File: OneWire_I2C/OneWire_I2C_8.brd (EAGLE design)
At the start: 25.4 x 35.6 mm, 25 parts, among them U1 P82B715D

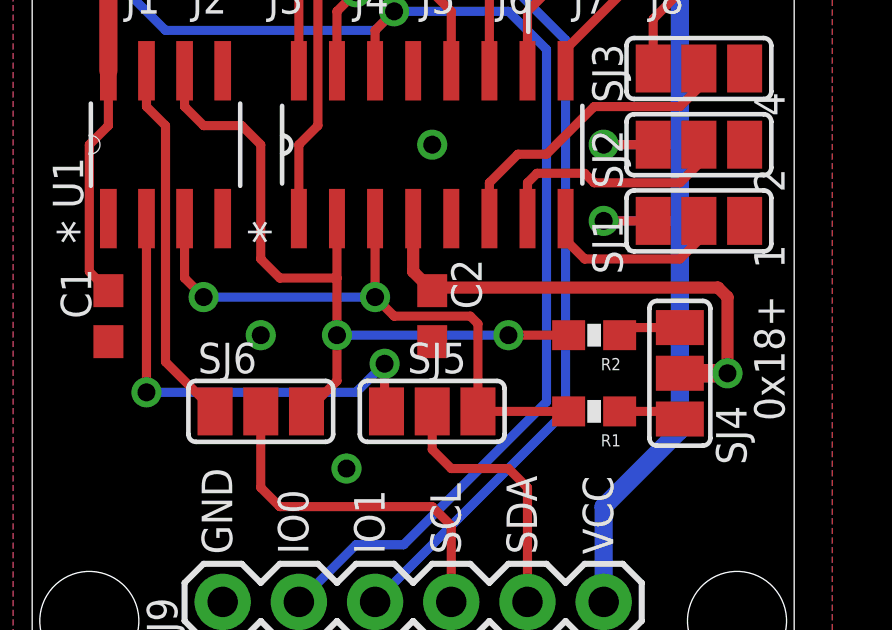
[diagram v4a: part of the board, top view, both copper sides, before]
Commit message: Added Raspberry pi board, updated I2C extender pullup resistors to other boards
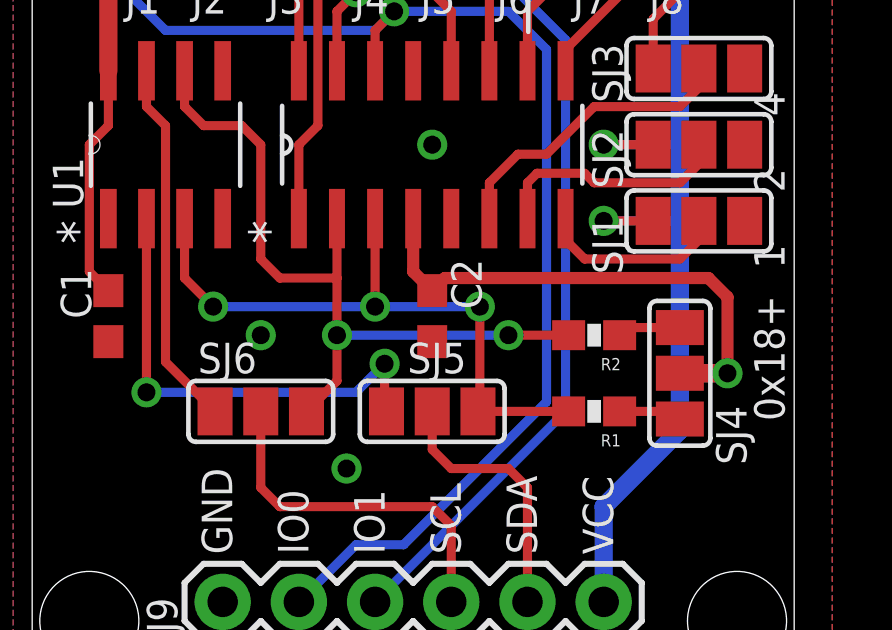
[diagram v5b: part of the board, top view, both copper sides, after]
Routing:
- net SDA: track 21.0 -> 21.7 mm, vias 2 -> 3
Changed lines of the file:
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@@
 <grid distance="0.025" unitdist="inch" unit="inch" style="dots" multiple="1" display="yes" altdistance="0.0125" altunitdist="inch" altunit="inch"/>
 <layers>
-<layer number="1" name="Top" color="4" fill="1" visible="no" active="yes"/>
+<layer number="1" name="Top" color="4" fill="1" visible="yes" active="yes"/>
 <layer number="2" name="Route2" color="1" fill="3" visible="no" active="no"/>
 <layer number="3" name="Route3" color="4" fill="3" visible="no" active="no"/>
@@
 <layer number="19" name="Unrouted" color="6" fill="1" visible="yes" active="yes"/>
 <layer number="20" name="Dimension" color="15" fill="1" visible="yes" active="yes"/>
-<layer number="21" name="tPlace" color="7" fill="1" visible="no" active="yes"/>
+<layer number="21" name="tPlace" color="7" fill="1" visible="yes" active="yes"/>
 <layer number="22" name="bPlace" color="7" fill="1" visible="yes" active="yes"/>
 <layer number="23" name="tOrigins" color="15" fill="1" visible="yes" active="yes"/>
@@
 <layer number="49" name="Reference" color="7" fill="1" visible="no" active="yes"/>
 <layer number="50" name="dxf" color="7" fill="1" visible="no" active="no"/>
-<layer number="51" name="tDocu" color="14" fill="1" visible="yes" active="yes"/>
+<layer number="51" name="tDocu" color="14" fill="1" visible="no" active="yes"/>
 <layer number="52" name="bDocu" color="7" fill="1" visible="yes" active="yes"/>
 <layer number="53" name="tGND_GNDA" color="7" fill="9" visible="no" active="no"/>
@@
 <via x="19.05" y="15.24" extent="1-16" drill="0.6"/>
 <wire x1="19.05" y1="15.24" x2="21.59" y2="15.24" width="0.3048" layer="16"/>
-<wire x1="22.86" y1="13.0175" x2="23.1775" y2="12.7" width="0.4064" layer="1"/>
+<wire x1="22.5425" y1="13.335" x2="23.1775" y2="12.7" width="0.4064" layer="1"/>
 <wire x1="23.1775" y1="12.7" x2="23.1775" y2="10.16" width="0.4064" layer="1"/>
 <wire x1="1.905" y1="17.78" x2="2.54" y2="18.415" width="0.3048" layer="1"/>
@@
 <wire x1="20.701" y1="21.971" x2="20.701" y2="20.32" width="0.3048" layer="1"/>
 <contactref element="C2" pad="1"/>
-<wire x1="22.86" y1="13.0175" x2="13.4375" y2="13.0175" width="0.4064" layer="1"/>
-<wire x1="13.4375" y1="13.0175" x2="13.335" y2="12.915" width="0.4064" layer="1"/>
+<wire x1="22.5425" y1="13.335" x2="13.755" y2="13.335" width="0.4064" layer="1"/>
+<wire x1="13.755" y1="13.335" x2="13.335" y2="12.915" width="0.4064" layer="1"/>
 <wire x1="12.7" y1="15.3162" x2="12.7" y2="13.55" width="0.4064" layer="1"/>
 <wire x1="12.7" y1="13.55" x2="13.335" y2="12.915" width="0.4064" layer="1"/>
@@
 <contactref element="R1" pad="2"/>
 <wire x1="17.8825" y1="8.89" x2="14.859" y2="8.89" width="0.3048" layer="1"/>
-<wire x1="14.859" y1="8.89" x2="14.859" y2="11.811" width="0.3048" layer="1"/>
-<wire x1="14.859" y1="11.811" x2="14.605" y2="12.065" width="0.3048" layer="1"/>
-<wire x1="14.605" y1="12.065" x2="12.065" y2="12.065" width="0.3048" layer="1"/>
-<wire x1="12.065" y1="12.065" x2="11.43" y2="12.7" width="0.3048" layer="1"/>
-<via x="11.43" y="12.7" extent="1-16" drill="0.6"/>
-<wire x1="11.43" y1="12.7" x2="5.715" y2="12.7" width="0.3048" layer="16"/>
-<via x="5.715" y="12.7" extent="1-16" drill="0.6"/>
-<wire x1="5.715" y1="12.7" x2="5.08" y2="13.335" width="0.3048" layer="1"/>
+<via x="11.43" y="12.3825" extent="1-16" drill="0.6"/>
+<wire x1="11.43" y1="12.3825" x2="6.0325" y2="12.3825" width="0.3048" layer="16"/>
+<via x="6.0325" y="12.3825" extent="1-16" drill="0.6"/>
+<wire x1="6.0325" y1="12.3825" x2="5.08" y2="13.335" width="0.3048" layer="1"/>
 <wire x1="5.08" y1="13.335" x2="5.08" y2="15.3162" width="0.3048" layer="1"/>
-<wire x1="11.43" y1="15.3162" x2="11.43" y2="12.7" width="0.3048" layer="1"/>
+<wire x1="11.43" y1="15.3162" x2="11.43" y2="12.3825" width="0.3048" layer="1"/>
+<wire x1="11.43" y1="12.3825" x2="14.9225" y2="12.3825" width="0.3048" layer="16"/>
+<via x="14.9225" y="12.3825" extent="1-16" drill="0.6"/>
+<wire x1="14.9225" y1="12.3825" x2="14.9225" y2="8.9535" width="0.3048" layer="1"/>
+<wire x1="14.9225" y1="8.9535" x2="14.859" y2="8.89" width="0.3048" layer="1"/>
 </signal>
 <signal name="SCL">

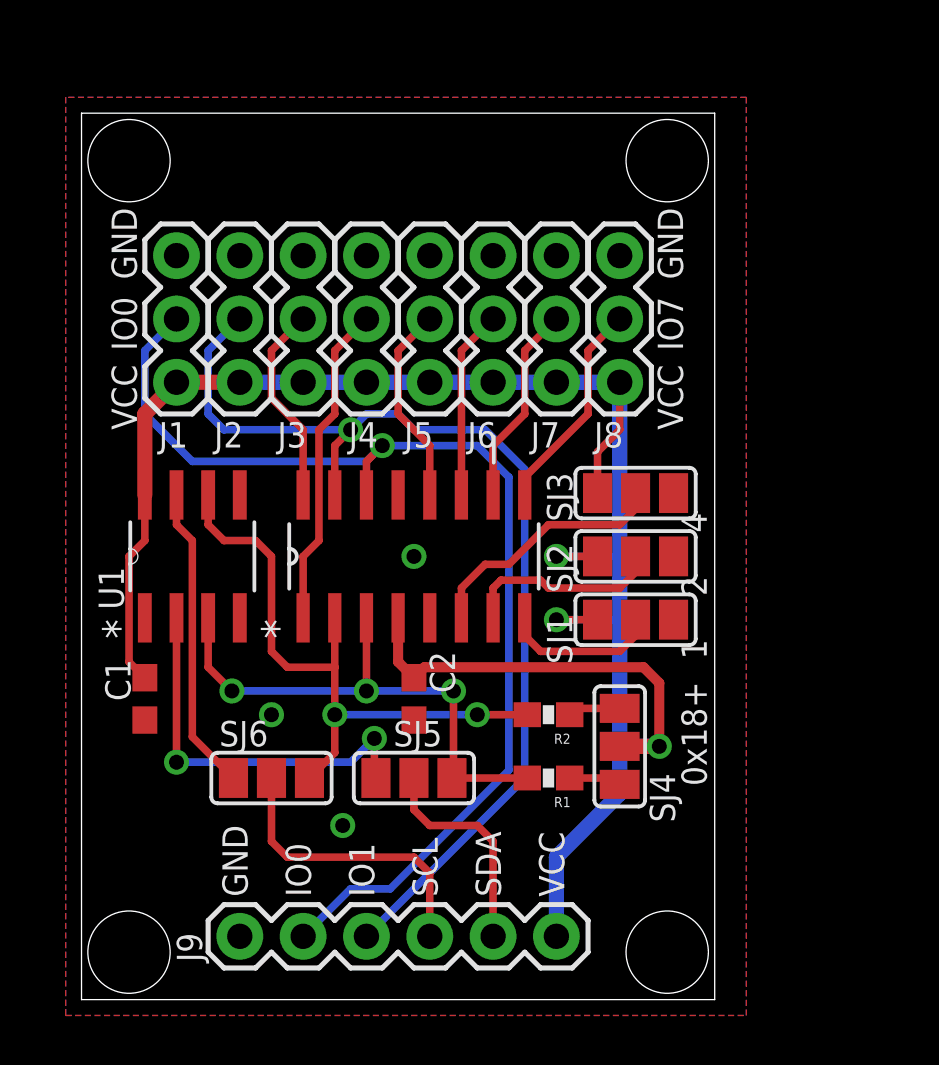
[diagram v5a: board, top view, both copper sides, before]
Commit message: Enlarged board, added regulator, replaced header with push connectors
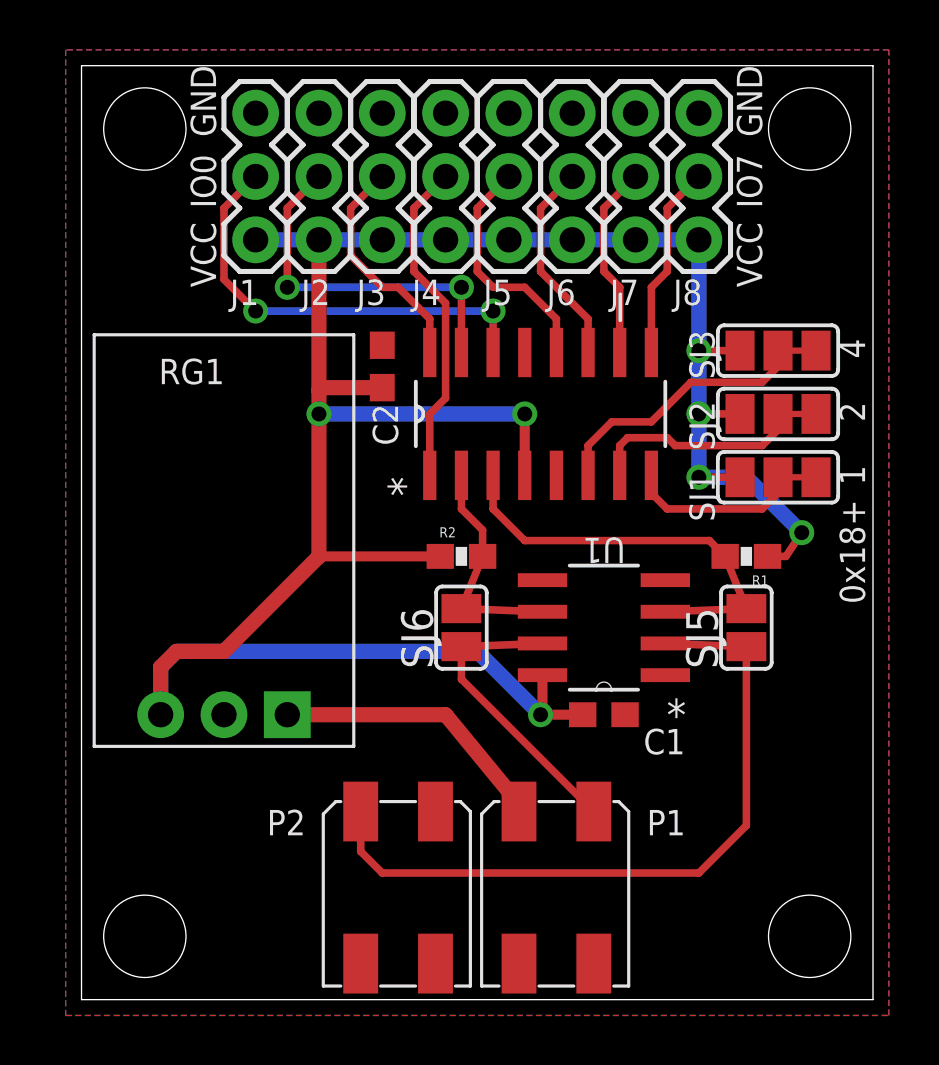
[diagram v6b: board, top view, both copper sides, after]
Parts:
- removed J9: (no value), SparkFun-Connectors:1X06
- removed SJ4: (no value), jumper:SJ_2
- added P1, P2: MOLEX_MINILITE_TRAP_2, Puffin:MOLEX_MINILITE_TRAP_2
- added RG1: (no value), Puffin:MURATA_REG_HOR
- SJ5, SJ6: device jumper:SJ_2 -> jumper:SJ
- moved C1 18.4 mm to (21.0, 11.4), turned to 0 degrees
- moved U1 16.8 mm to (21.0, 14.9), turned to 180 degrees
- moved SJ5 14.6 mm to (26.7, 14.9), turned to 90 degrees
- moved C2 13.4 mm to (12.1, 25.4), turned to 90 degrees
- moved R1 11.9 mm to (26.7, 17.8)
- moved SJ6 9.72 mm to (15.2, 14.9), turned to 90 degrees
- moved SJ2 8.08 mm to (27.9, 23.5)
- moved SJ3 8.08 mm to (27.9, 26.0)
- moved SJ1 8.08 mm to (27.9, 21.0)
- moved W1 7.65 mm to (18.4, 23.5)
- moved R2 7.25 mm to (15.2, 17.8), turned to 0 degrees
- moved J1 6.54 mm to (6.99, 30.5)
- moved J2 6.54 mm to (9.53, 30.5)
- moved J4 6.54 mm to (14.6, 30.5)
- moved J7 6.54 mm to (22.2, 30.5)
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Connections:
- removed net LSCL: J9.4, SJ6.2
- removed net LSDA: J9.5, SJ5.2
- removed net LX: SJ5.1, U1.2
- removed net N$1: R2.1, SJ4.3
- removed net N$2: R1.1, SJ4.1
- new net IN: P1.2, RG1.1
- new net N$3: P2.2, SJ5.1, U1.2
- net GND: now also P2.1, RG1.2; no longer J9.1
- net IO0: no longer J9.2
- net IO1: no longer J9.3
- net LY: now also P1.1
- net SCL: now also SJ6.2; no longer SJ6.3
- net SDA: now also SJ5.2; no longer SJ5.3
- net VCC: now also R1.1, R2.1, RG1.3; no longer J9.6, SJ4.2
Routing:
- net N$3: track 0.00 -> 28.6 mm
- net IO1: track 42.7 -> 14.6 mm, vias 1 -> 2
- net IO0: track 45.5 -> 17.6 mm, vias 1 -> 2
- net SCL: track 25.4 -> 9.12 mm, vias 2 -> 0
- net VCC: track 85.8 -> 101.9 mm, vias 3 -> 7
- net LX: track 16.0 -> 0.00 mm, vias 2 -> 0
- net LSCL: track 12.0 -> 0.00 mm
- net IN: track 0.00 -> 11.3 mm
- net LSDA: track 8.78 -> 0.00 mm
- net SDA: track 21.7 -> 17.0 mm, vias 3 -> 0
- net N$2: track 2.49 -> 0.00 mm
- net N$1: track 2.11 -> 0.00 mm
- net AD1: track 8.07 -> 9.97 mm
- net AD2: track 10.1 -> 12.0 mm
- net AD0: track 6.32 -> 8.22 mm
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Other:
- board size 25.4 x 35.6 mm -> 31.8 x 37.5 mm
- board text added: "VIN"
- board text removed: "IO1"

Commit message: Gate 4, and misc updates
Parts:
- moved U$1 0.64 mm to (2.54, 35.6)
- moved U$4 0.64 mm to (29.2, 35.6)
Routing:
- net AD2: track 12.0 -> 10.8 mm
- net AD1: track 9.97 -> 8.70 mm
- net AD0: track 8.22 -> 6.95 mm
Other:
- board size 31.8 x 37.5 mm -> 31.8 x 38.1 mm
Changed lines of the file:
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@@
 <plain>
 <wire x1="0" y1="0" x2="31.75" y2="0" width="0" layer="20"/>
-<wire x1="31.75" y1="0" x2="31.75" y2="37.465" width="0" layer="20"/>
-<wire x1="31.75" y1="37.465" x2="0" y2="37.465" width="0" layer="20"/>
-<wire x1="0" y1="37.465" x2="0" y2="0" width="0" layer="20"/>
-<text x="5.3975" y="31.75" size="1.016" layer="21" font="vector" ratio="15" rot="R90">IO0</text>
-<text x="27.305" y="31.75" size="1.016" layer="21" font="vector" ratio="15" rot="R90">IO7</text>
-<text x="5.3975" y="34.6075" size="1.016" layer="21" font="vector" ratio="15" rot="R90">GND</text>
-<text x="5.3975" y="28.575" size="1.016" layer="21" font="vector" ratio="15" rot="R90">VCC</text>
-<text x="27.305" y="28.575" size="1.016" layer="21" font="vector" ratio="15" rot="R90">VCC</text>
-<text x="27.305" y="34.6075" size="1.016" layer="21" font="vector" ratio="15" rot="R90">GND</text>
+<wire x1="31.75" y1="0" x2="31.75" y2="38.1" width="0" layer="20"/>
+<wire x1="31.75" y1="38.1" x2="0" y2="38.1" width="0" layer="20"/>
+<wire x1="0" y1="38.1" x2="0" y2="0" width="0" layer="20"/>
+<text x="3.175" y="32.0675" size="1.016" layer="21" font="vector" ratio="15">IO0</text>
+<text x="26.3525" y="32.0675" size="1.016" layer="21" font="vector" ratio="15">IO7</text>
+<text x="5.715" y="34.29" size="1.016" layer="21" font="vector" ratio="15" rot="R90">GND</text>
+<text x="2.8575" y="29.845" size="1.016" layer="21" font="vector" ratio="15">VCC</text>
+<text x="26.3525" y="29.845" size="1.016" layer="21" font="vector" ratio="15">VCC</text>
+<text x="26.9875" y="34.29" size="1.016" layer="21" font="vector" ratio="15" rot="R90">GND</text>
 <text x="31.4325" y="25.7175" size="1.016" layer="21" font="vector" ratio="15" rot="R90">4</text>
 <text x="31.4325" y="20.6375" size="1.016" layer="21" font="vector" ratio="15" rot="R90">1</text>
@@
 <text x="10.795" y="3.175" size="1.016" layer="22" font="vector" ratio="15" rot="MR90">SDA</text>
 <text x="17.145" y="3.175" size="1.016" layer="22" font="vector" ratio="15" rot="MR90">VIN</text>
-<text x="26.3525" y="28.575" size="1.016" layer="22" font="vector" ratio="15" rot="MR90">VCC</text>
-<text x="4.445" y="28.575" size="1.016" layer="22" font="vector" ratio="15" rot="MR90">VCC</text>
-<text x="4.445" y="34.6075" size="1.016" layer="22" font="vector" ratio="15" rot="MR90">GND</text>
-<text x="26.3525" y="34.6075" size="1.016" layer="22" font="vector" ratio="15" rot="MR90">GND</text>
-<text x="4.445" y="31.75" size="1.016" layer="22" font="vector" ratio="15" rot="MR90">IO0</text>
-<text x="26.3525" y="31.75" size="1.016" layer="22" font="vector" ratio="15" rot="MR90">IO7</text>
+<text x="28.8925" y="29.845" size="1.016" layer="22" font="vector" ratio="15" rot="MR0">VCC</text>
+<text x="5.3975" y="29.845" size="1.016" layer="22" font="vector" ratio="15" rot="MR0">VCC</text>
+<text x="4.7625" y="34.29" size="1.016" layer="22" font="vector" ratio="15" rot="MR90">GND</text>
+<text x="26.035" y="34.29" size="1.016" layer="22" font="vector" ratio="15" rot="MR90">GND</text>
+<text x="5.3975" y="32.0675" size="1.016" layer="22" font="vector" ratio="15" rot="MR0">IO0</text>
+<text x="28.575" y="32.0675" size="1.016" layer="22" font="vector" ratio="15" rot="MR0">IO7</text>
 <text x="15.5575" y="22.225" size="0.4064" layer="51" font="vector" ratio="15" rot="R90">SCL</text>
 <text x="16.8275" y="22.225" size="0.4064" layer="51" font="vector" ratio="15" rot="R90">SDA</text>
+<circle x="20.5105" y="9.3345" radius="0.2794" width="0.508" layer="21"/>
+<circle x="17.5895" y="9.3345" radius="0.359209375" width="0.254" layer="21"/>
+<circle x="11.176" y="9.3345" radius="0.359209375" width="0.254" layer="21"/>
+<circle x="14.224" y="9.3345" radius="0.2794" width="0.508" layer="21"/>
 </plain>
 <attributes>
@@
 <attribute name="VALUE" x="27.94" y="29.21" size="1.27" layer="27" rot="R90"/>
 </element>
-<element name="R1" library="SparkFun-Passives" package="0603-RES" value="" x="26.67" y="17.78" rot="R180"/>
-<element name="R2" library="SparkFun-Passives" package="0603-RES" value="" x="15.24" y="17.78"/>
+<element name="R1" library="SparkFun-Passives" package="0603-RES" value="" x="26.67" y="17.78" smashed="yes" rot="R180">
+<attribute name="NAME" x="27.559" y="19.558" size="1.016" layer="25" font="vector" ratio="15" rot="R180"/>
+<attribute name="VALUE" x="27.686" y="18.923" size="0.4064" layer="27" font="vector" rot="R180"/>
+</element>
+<element name="R2" library="SparkFun-Passives" package="0603-RES" value="" x="15.24" y="17.78" smashed="yes">
+<attribute name="NAME" x="14.351" y="18.542" size="1.016" layer="25" font="vector" ratio="15"/>
+<attribute name="VALUE" x="14.224" y="16.637" size="0.4064" layer="27" font="vector"/>
+</element>
 <element name="SJ1" library="jumper" package="SJ_2" value="" x="27.94" y="20.955" smashed="yes">
-<attribute name="NAME" x="25.4" y="19.177" size="1.016" layer="25" font="vector" ratio="15" rot="R90"/>
 <attribute name="VALUE" x="27.8399" y="20.955" size="0.02" layer="27"/>
 </element>
 <element name="SJ2" library="jumper" package="SJ_2" value="" x="27.94" y="23.495" smashed="yes">
-<attribute name="NAME" x="25.4" y="22.0345" size="1.016" layer="25" font="vector" ratio="15" rot="R90"/>
 <attribute name="VALUE" x="27.8399" y="23.495" size="0.02" layer="27"/>
 </element>
 <element name="SJ3" library="jumper" package="SJ_2" value="" x="27.94" y="26.035" smashed="yes">
-<attribute name="NAME" x="25.4" y="24.892" size="1.016" layer="25" font="vector" ratio="15" rot="R90"/>
 <attribute name="VALUE" x="27.8399" y="26.035" size="0.02" layer="27"/>
 </element>
@@
 <attribute name="SUPPLIER" value="Texas Instruments" x="20.955" y="14.9225" size="1.778" layer="27" rot="R180" display="off"/>
 <attribute name="OC_FARNELL" value="1604945" x="20.955" y="14.9225" size="1.778" layer="27" rot="R180" display="off"/>
-<attribute name="NAME" x="21.8186" y="18.5293" size="1.016" layer="25" font="vector" ratio="15" rot="SR180"/>
+<attribute name="NAME" x="20.0914" y="17.6657" size="1.016" layer="25" font="vector" ratio="15" rot="SR0"/>
 </element>
 <element name="C2" library="resistor" package="C0603" value="" x="12.065" y="25.4" smashed="yes" rot="R90">
@@
 <attribute name="VALUE" x="13.97" y="24.765" size="1.27" layer="27" rot="R90"/>
 </element>
-<element name="U$1" library="SparkFun-Electromechanical" package="STAND-OFF" value="" x="2.54" y="34.925"/>
-<element name="U$4" library="SparkFun-Electromechanical" package="STAND-OFF" value="" x="29.21" y="34.925"/>
-<element name="RG1" library="Puffin" package="MURATA_REG_HOR" value="" x="5.715" y="11.43"/>
+<element name="U$1" library="SparkFun-Electromechanical" package="STAND-OFF" value="" x="2.54" y="35.56"/>
+<element name="U$4" library="SparkFun-Electromechanical" package="STAND-OFF" value="" x="29.21" y="35.56"/>
+<element name="RG1" library="Puffin" package="MURATA_REG_HOR" value="" x="5.715" y="11.43" smashed="yes">
+<attribute name="NAME" x="1.1938" y="8.8138" size="1.016" layer="25" font="vector" ratio="15"/>
+<attribute name="VALUE" x="3.175" y="18.415" size="1.016" layer="27" font="vector" ratio="15"/>
+</element>
 <element name="P1" library="Puffin" package="MOLEX_MINILITE_TRAP_2" value="MOLEX_MINILITE_TRAP_2" x="19.05" y="4.445" smashed="yes" rot="R270">
 <attribute name="NAME" x="22.6775" y="6.5925" size="1.016" layer="21" font="vector" ratio="15"/>
@@
 <attribute name="NAME" x="7.4375" y="6.5925" size="1.016" layer="21" font="vector" ratio="15"/>
 </element>
-<element name="SJ5" library="jumper" package="SJ" value="" x="26.67" y="14.9225" rot="R90"/>
-<element name="SJ6" library="jumper" package="SJ" value="" x="15.24" y="14.9225" rot="R90"/>
+<element name="SJ5" library="jumper" package="SJ" value="" x="26.67" y="14.9225" smashed="yes" rot="R90">
+<attribute name="NAME" x="25.527" y="13.2715" size="1.016" layer="25" ratio="15" rot="R90"/>
+<attribute name="VALUE" x="26.67" y="15.3226" size="0.02" layer="27" rot="R90"/>
+</element>
+<element name="SJ6" library="jumper" package="SJ" value="" x="15.24" y="14.9225" smashed="yes" rot="R90">
+<attribute name="NAME" x="14.097" y="13.2715" size="1.016" layer="25" ratio="15" rot="R90"/>
+<attribute name="VALUE" x="15.24" y="15.3226" size="0.02" layer="27" rot="R90"/>
+</element>
 </elements>
 <signals>
@@
 <wire x1="27.305" y1="22.225" x2="27.94" y2="22.86" width="0.3048" layer="1"/>
 <wire x1="27.94" y1="22.86" x2="27.94" y2="23.495" width="0.3048" layer="1"/>
-<wire x1="27.94" y1="23.495" x2="29.21" y2="23.495" width="0.254" layer="1"/>
 </signal>
 <signal name="AD2">
@@
 <wire x1="21.2725" y1="23.1775" x2="20.32" y2="22.225" width="0.3048" layer="1"/>
 <wire x1="20.32" y1="22.225" x2="20.32" y2="21.0312" width="0.3048" layer="1"/>
-<wire x1="27.94" y1="26.035" x2="29.21" y2="26.035" width="0.254" layer="1"/>
 </signal>
 <signal name="SDA">
@@
 <wire x1="23.495" y1="19.685" x2="22.86" y2="20.32" width="0.3048" layer="1"/>
 <wire x1="22.86" y1="20.32" x2="22.86" y2="21.0312" width="0.3048" layer="1"/>
-<wire x1="27.94" y1="20.955" x2="29.21" y2="20.955" width="0.254" layer="1"/>
 </signal>
 <signal name="LY">
